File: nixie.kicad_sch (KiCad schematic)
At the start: 15 parts, among them Q1 2N3906, Q2 Q_NMOS_GDS, U1 MC34063AP

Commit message: updated power
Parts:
- added J1: Barrel_Jack, symbol Connector:Barrel_Jack
- added U2: LM7805_TO220, Package_TO_SOT_THT:TO-220-3_Vertical, symbol Regulator_Linear:LM7805_TO220
- C1: value C -> 447p
- D3: value D_TVS -> 220
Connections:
- net GND: now also J1.2, U2.2 (GND)
- net Vin: now also J1.1, U2.1 (VI)
- net V_HV renamed HV
- new net 5V: U2.3 (VO)
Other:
- note added: "Power Input 12V Output 5V and 190V"
- moved on the sheet: C1, C2, C3, D1, D2, D3, L1, Q1, Q2, R1, R2, R3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

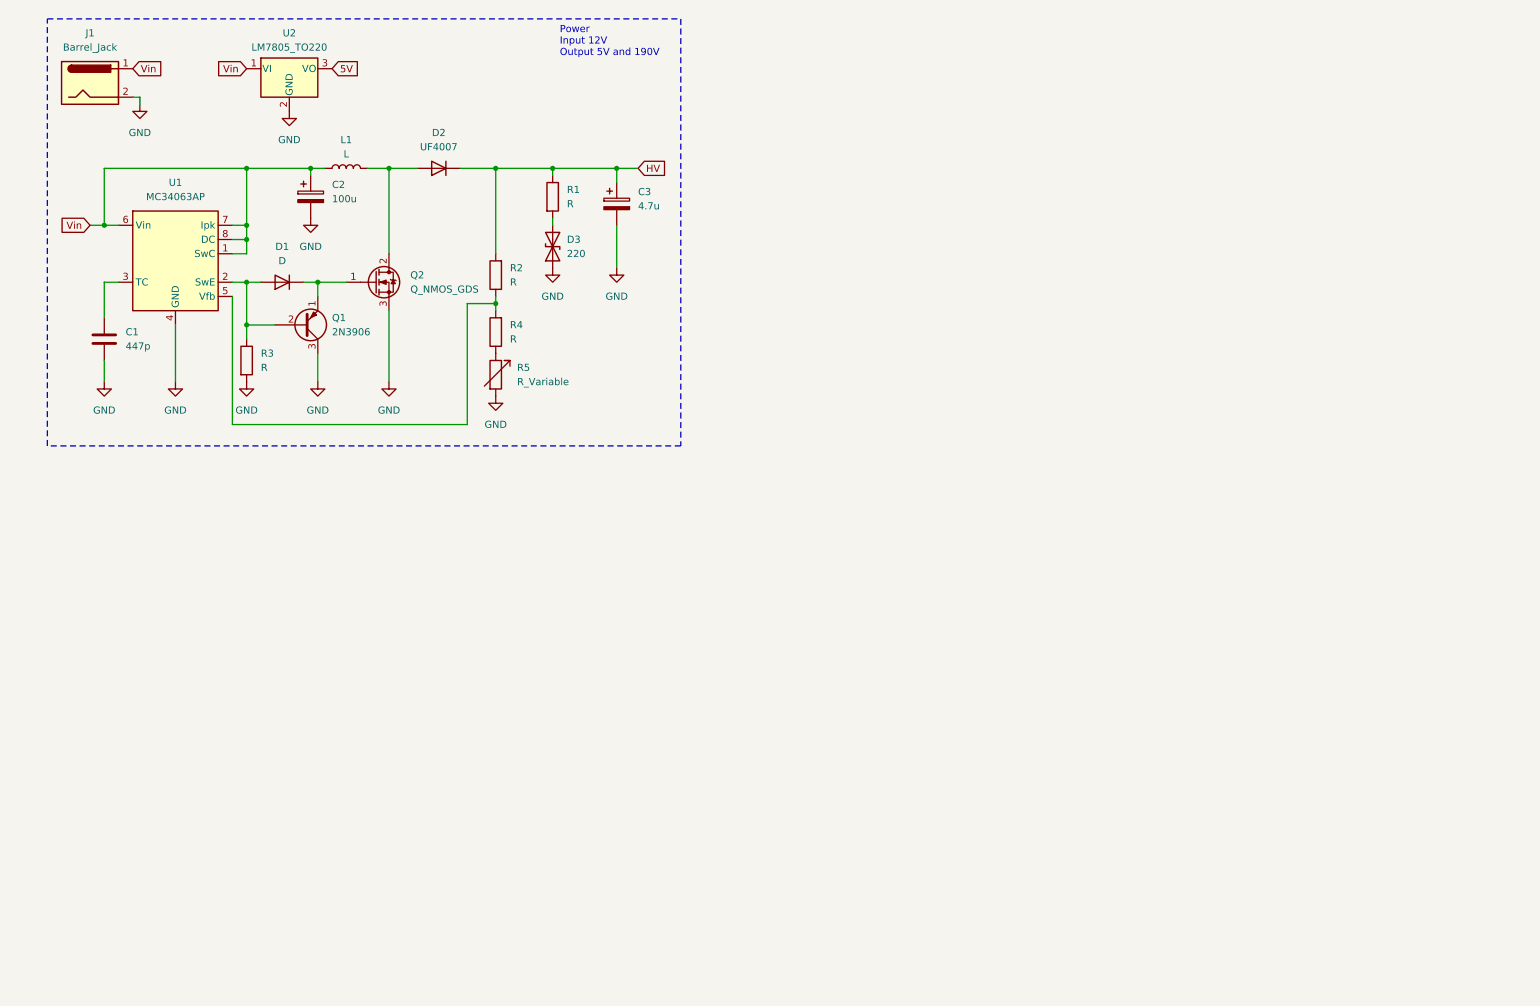
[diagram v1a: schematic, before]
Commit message: stub with nixies and drivers
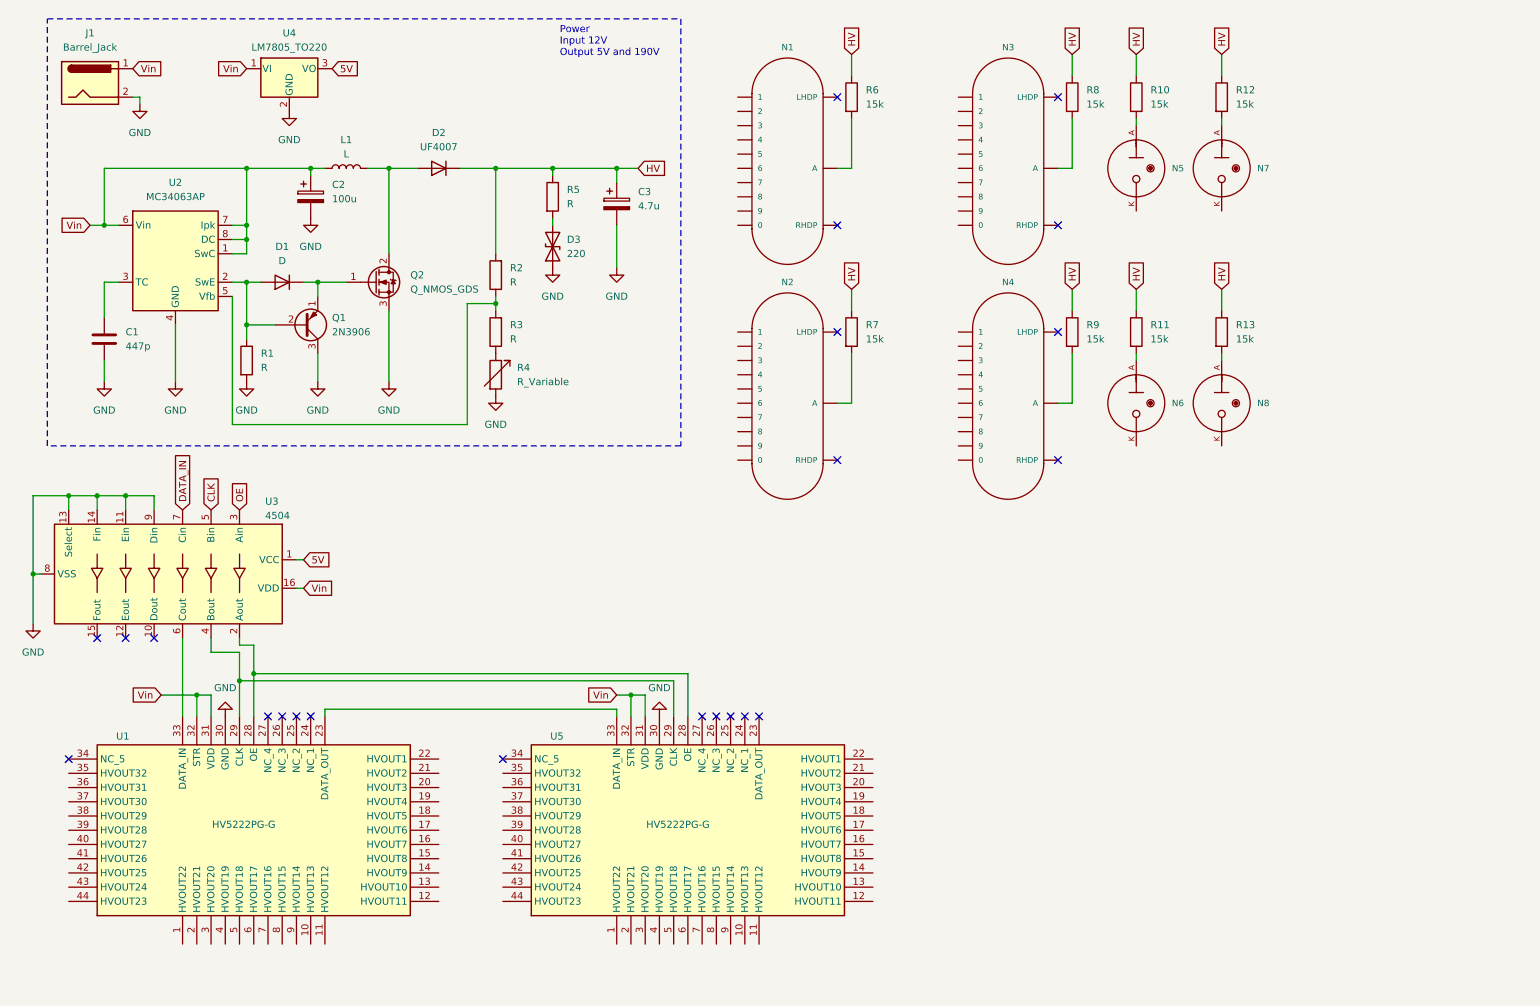
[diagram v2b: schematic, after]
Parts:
- added N1, N2, N3, N4: IN-14, nixie:nixies-us-IN-14, symbol nixie:IN-14
- added N5, N6, N7, N8: IN-3, nixie:nixies-us-IN-3, symbol nixie:IN-3
- added R10, R11, R12, R13, R6, R7, R8, R9: 15k, symbol Device:R
- added U1, U5: HV5222PG-G, Package_QFP:PQFP-44_10x10mm_P0.8mm, symbol nixie:HV5222PG-G
- added U3: 4504, Package_DIP:DIP-16_W7.62mm, symbol 4xxx:4504
- renumbered R3 to R1, R4 to R3, R5 to R4, R1 to R5, U1 to U2, U2 to U4
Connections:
- net 5V: now also U3.1 (VCC)
- net GND: now also U1.30 (GND), U3.11 (Ein), U3.13 (Select), U3.14 (Fin), U3.8 (VSS), U3.9 (Din), U5.30 (GND)
- net HV: now also R10.1, R11.1, R12.1, R13.1, R6.1, R7.1, R8.1, R9.1
- net Vin: now also U1.31 (VDD), U1.32 (STR), U3.16 (VDD), U5.31 (VDD), U5.32 (STR)
- new net: N1.A, R6.2
- new net: N7.A, R12.2
- new net: N6.A, R11.2
- new net: N2.A, R7.2
- new net: U1.23 (DATA_OUT), U5.33 (DATA_IN)
- new net: U1.28 (OE), U3.2 (Aout), U5.28 (OE)
- new net: U1.29 (CLK), U3.4 (Bout), U5.29 (CLK)
- new net: U1.33 (DATA_IN), U3.6 (Cout)
- new net: N3.A, R8.2
- new net: N8.A, R13.2
- new net: N5.A, R10.2
- new net: N4.A, R9.2
- new net CLK: U3.5 (Bin)
- new net DATA_IN: U3.7 (Cin)
- new net OE: U3.3 (Ain)
- no-connect marks 0 -> 22

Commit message: connected nixie tubes, drivers, and level shifting
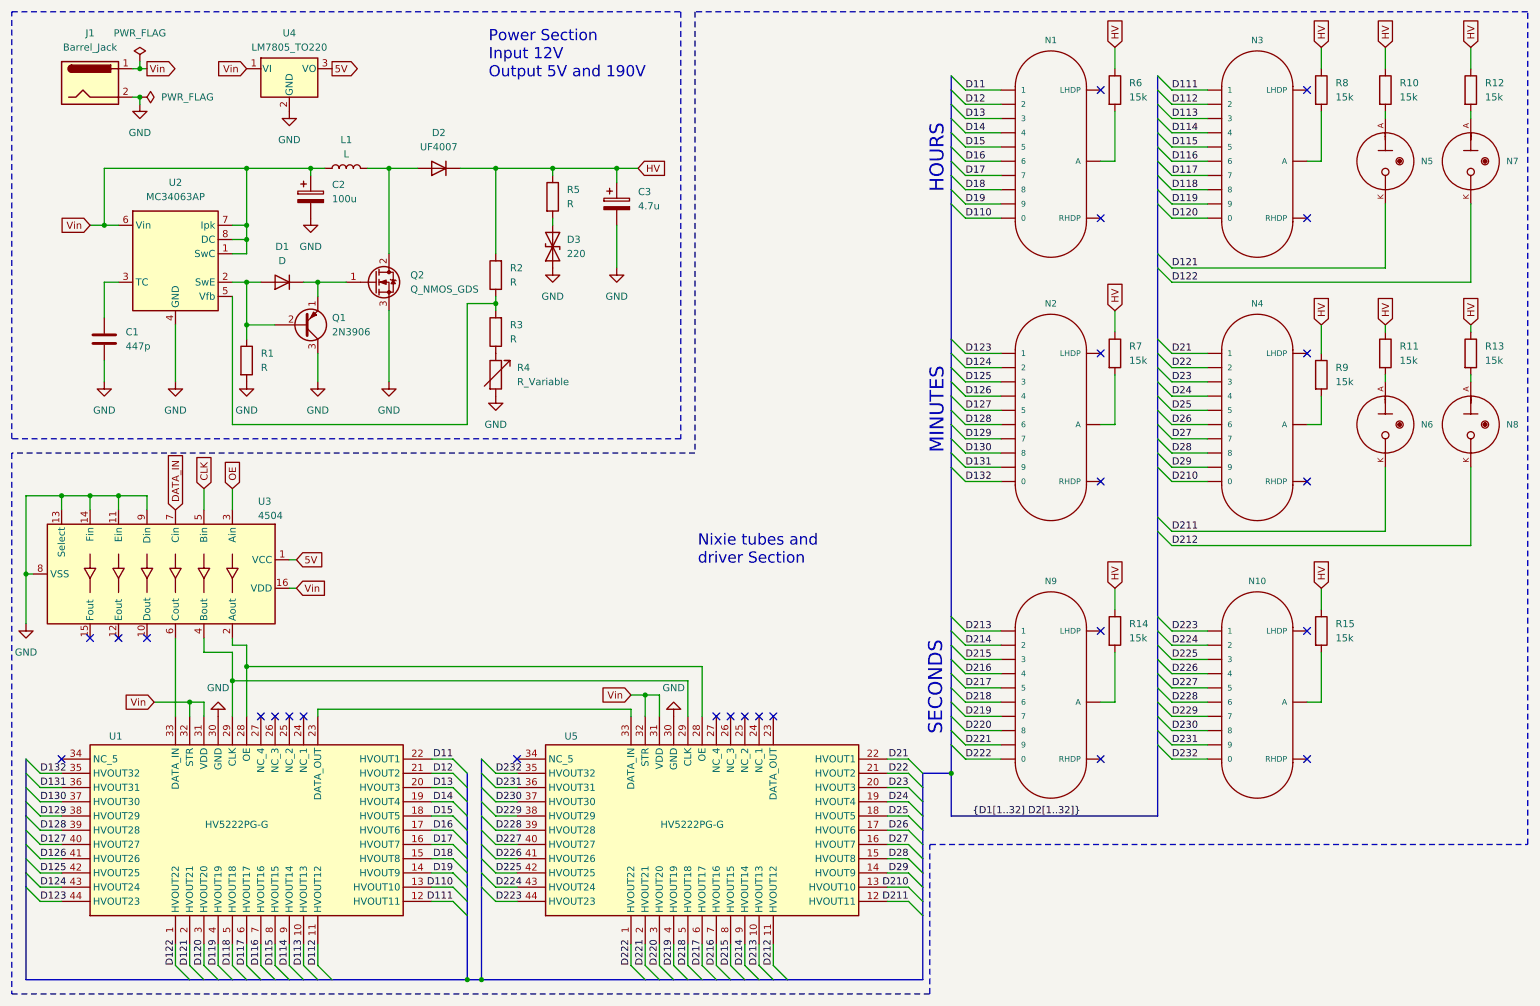
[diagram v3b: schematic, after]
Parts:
- added N10, N9: IN-14, nixie:nixies-us-IN-14, symbol nixie:IN-14
- added R14, R15: 15k, symbol Device:R
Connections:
- net HV: now also R14.1, R15.1
- net D110: now reaches N1.0
- net D110: now also U1.13 (HVOUT10)
- net D11: now reaches N1.1
- net D11: now also U1.22 (HVOUT1)
- net D12: now reaches N1.2
- net D12: now also U1.21 (HVOUT2)
- net D13: now reaches N1.3
- net D13: now also U1.20 (HVOUT3)
- net D14: now reaches N1.4
- net D14: now also U1.19 (HVOUT4)
- net D15: now reaches N1.5
- net D15: now also U1.18 (HVOUT5)
- net D16: now reaches N1.6
- net D16: now also U1.17 (HVOUT6)
- net D17: now reaches N1.7
- net D17: now also U1.16 (HVOUT7)
- net D18: now reaches N1.8
- net D18: now also U1.15 (HVOUT8)
- net D19: now reaches N1.9
- net D19: now also U1.14 (HVOUT9)
- net D211: now reaches N6.K
- net D211: now also U5.12 (HVOUT11)
- net D132: now reaches N2.0
- net D132: now also U1.35 (HVOUT32)
- net D123: now reaches N2.1
- net D123: now also U1.44 (HVOUT23)
- net D124: now reaches N2.2
- net D124: now also U1.43 (HVOUT24)
- net D125: now reaches N2.3
- net D125: now also U1.42 (HVOUT25)
- net D126: now reaches N2.4
- net D126: now also U1.41 (HVOUT26)
- net D127: now reaches N2.5
- net D127: now also U1.40 (HVOUT27)
- net D128: now reaches N2.6
- net D128: now also U1.39 (HVOUT28)
- net D129: now reaches N2.7
- net D129: now also U1.38 (HVOUT29)
- net D130: now reaches N2.8
- net D130: now also U1.37 (HVOUT30)
- net D131: now reaches N2.9
- net D131: now also U1.36 (HVOUT31)
- net D122: now reaches U1.1 (HVOUT22)
- net D122: now also N7.K
- net D113: now reaches U1.10 (HVOUT13)
- net D113: now also N3.3
- net D112: now reaches U1.11 (HVOUT12)
- net D112: now also N3.2
- net D111: now reaches U1.12 (HVOUT11)
- net D111: now also N3.1
- net D121: now reaches U1.2 (HVOUT21)
- net D121: now also N5.K
- net D120: now reaches U1.3 (HVOUT20)
- net D120: now also N3.0
- net D119: now reaches U1.4 (HVOUT19)
- net D119: now also N3.9
- net D118: now reaches U1.5 (HVOUT18)
- net D118: now also N3.8
- net D117: now reaches U1.6 (HVOUT17)
- net D117: now also N3.7
- net D116: now reaches U1.7 (HVOUT16)
- net D116: now also N3.6
- net D115: now reaches U1.8 (HVOUT15)
- net D115: now also N3.5
- net D114: now reaches U1.9 (HVOUT14)
- net D114: now also N3.4
- net D212: now reaches N8.K
- net D212: now also U5.11 (HVOUT12)
- net D210: now reaches N4.0
- net D210: now also U5.13 (HVOUT10)
- net D21: now reaches N4.1
- net D21: now also U5.22 (HVOUT1)
- net D22: now reaches N4.2
- net D22: now also U5.21 (HVOUT2)
- net D23: now reaches N4.3
- net D23: now also U5.20 (HVOUT3)
- net D24: now reaches N4.4
- net D24: now also U5.19 (HVOUT4)
- net D25: now reaches N4.5
- net D25: now also U5.18 (HVOUT5)
- net D26: now reaches N4.6
- net D26: now also U5.17 (HVOUT6)
- net D27: now reaches N4.7
- net D27: now also U5.16 (HVOUT7)
- net D28: now reaches N4.8
- net D28: now also U5.15 (HVOUT8)
- net D29: now reaches N4.9
- net D29: now also U5.14 (HVOUT9)
- net D222: now reaches U5.1 (HVOUT22)
- net D222: now also N9.0
- net D213: now reaches U5.10 (HVOUT13)
- net D213: now also N9.1
- net D221: now reaches U5.2 (HVOUT21)
- net D221: now also N9.9
- net D220: now reaches U5.3 (HVOUT20)
- net D220: now also N9.8
- net D232: now reaches U5.35 (HVOUT32)
- net D232: now also N10.0
- net D231: now reaches U5.36 (HVOUT31)
- net D231: now also N10.9
- net D230: now reaches U5.37 (HVOUT30)
- net D230: now also N10.8
- net D229: now reaches U5.38 (HVOUT29)
- net D229: now also N10.7
- net D228: now reaches U5.39 (HVOUT28)
- net D228: now also N10.6
- net D219: now reaches U5.4 (HVOUT19)
- net D219: now also N9.7
- net D227: now reaches U5.40 (HVOUT27)
- net D227: now also N10.5
- net D226: now reaches U5.41 (HVOUT26)
- net D226: now also N10.4
- net D225: now reaches U5.42 (HVOUT25)
- net D225: now also N10.3
- net D224: now reaches U5.43 (HVOUT24)
- net D224: now also N10.2
- net D223: now reaches U5.44 (HVOUT23)
- net D223: now also N10.1
- net D218: now reaches U5.5 (HVOUT18)
- net D218: now also N9.6
- net D217: now reaches U5.6 (HVOUT17)
- net D217: now also N9.5
- net D216: now reaches U5.7 (HVOUT16)
- net D216: now also N9.4
- net D215: now reaches U5.8 (HVOUT15)
- net D215: now also N9.3
- net D214: now reaches U5.9 (HVOUT14)
- net D214: now also N9.2
- new net: N10.A, R15.2
- new net: N9.A, R14.2
- no-connect marks 22 -> 26
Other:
- note added: "HOURS"
- note added: "MINUTES"
- note added: "Nixie tubes and driver Section"
- note added: "Power Section Input 12V Output 5V and 190V"
- note added: "SECONDS"
- note removed: "Power Input 12V Output 5V and 190V"
- moved on the sheet: N1, N2, N3, N4, N5, N6, N7, N8, R10, R11, R12, R13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

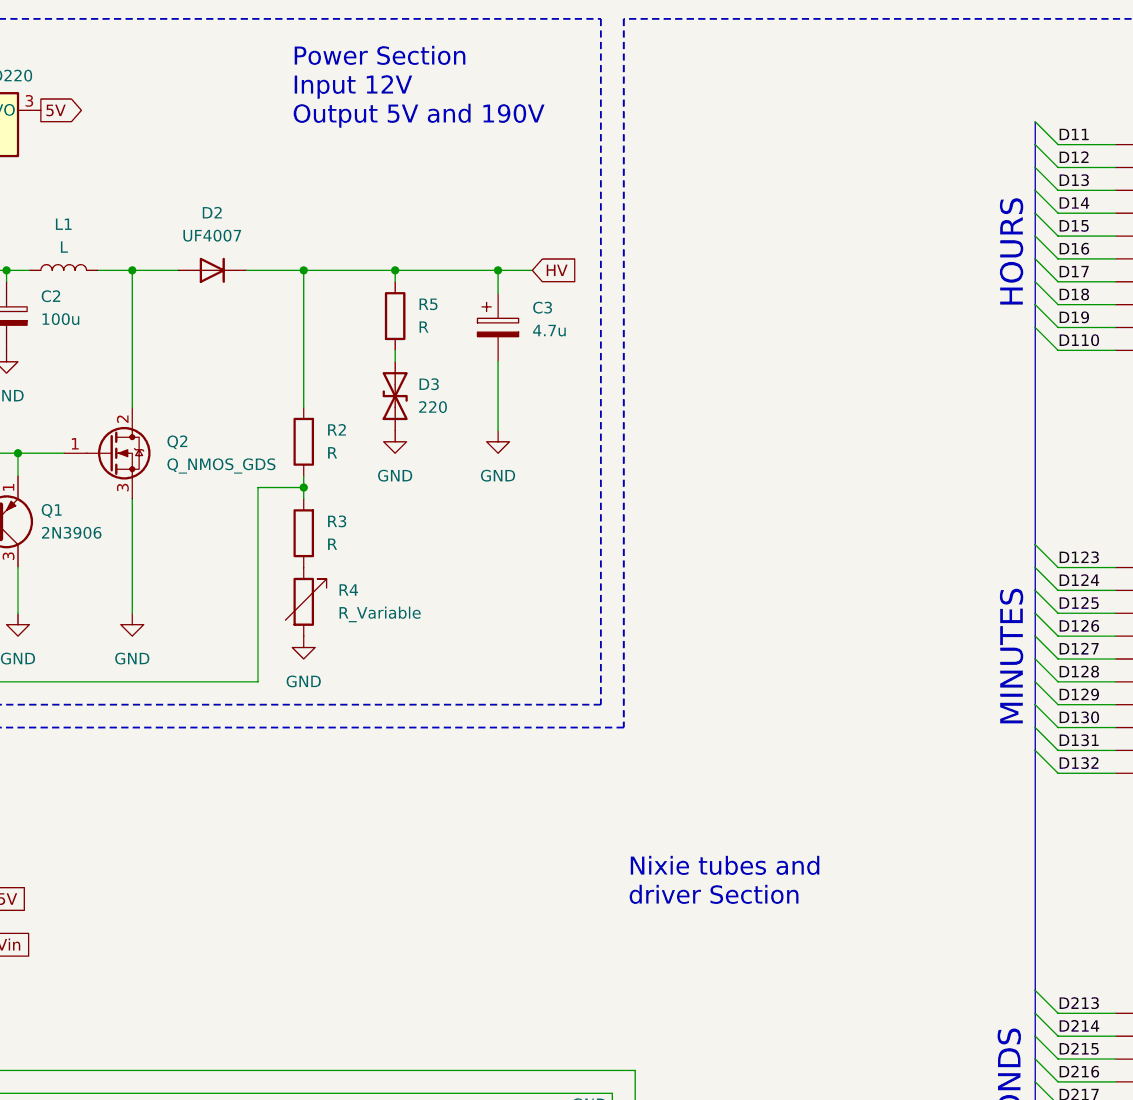
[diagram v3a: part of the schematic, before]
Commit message: added controller stub
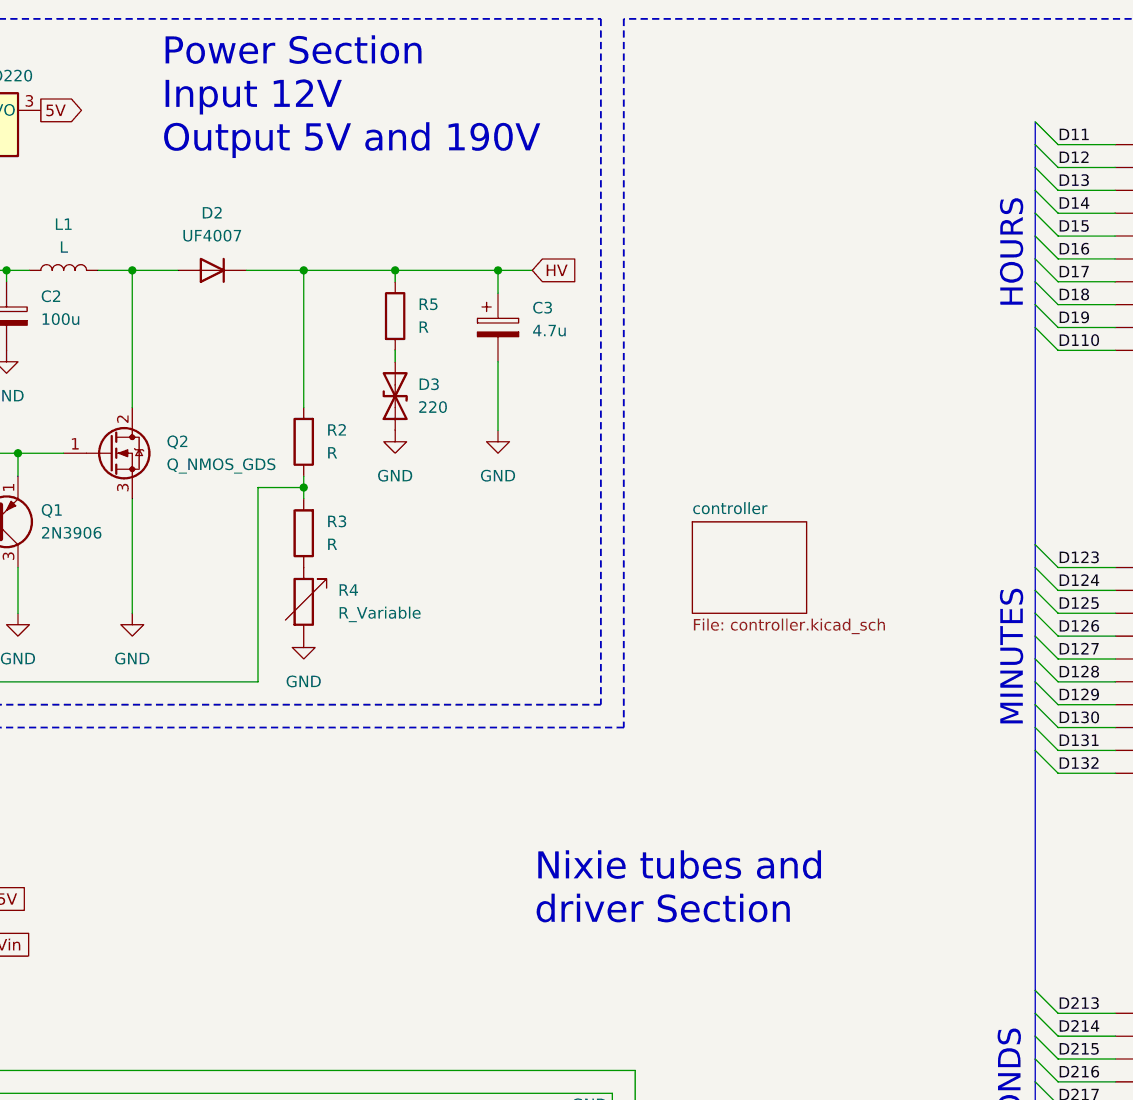
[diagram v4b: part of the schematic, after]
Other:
- added sheet controller (controller.kicad_sch)
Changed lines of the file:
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@@
 	(text "Power Section\nInput 12V\nOutput 5V and 190V"
 		(exclude_from_sim no)
-		(at 97.79 24.13 0)
+		(at 83.312 25.146 0)
 		(effects
 			(font
-				(size 2 2)
+				(size 3 3)
 			)
 			(justify left)
@@
 	(text "Nixie tubes and \ndriver Section"
 		(exclude_from_sim no)
-		(at 135.128 112.522 0)
+		(at 124.714 113.284 0)
 		(effects
 			(font
-				(size 2 2)
+				(size 3 3)
 			)
 			(justify left)
@@
 				)
 			)
+		)
+	)
+	(sheet
+		(at 142.24 72.39)
+		(size 12.7 10.16)
+		(fields_autoplaced yes)
+		(stroke
+			(width 0.1524)
+			(type solid)
+		)
+		(fill
+			(color 0 0 0 0.0000)
+		)
+		(property "Sheetname" "controller"
+			(at 142.24 71.6784 0)
+			(effects
+				(font
+					(size 1.27 1.27)
+				)
+				(justify left bottom)
+			)
+		)
+		(property "Sheetfile" "controller.kicad_sch"
+			(at 142.24 83.1346 0)
+			(effects
+				(font
+					(size 1.27 1.27)
+				)
+				(justify left top)
+			)
+		)
+		(instances
+			(project "nixie"
+				(path "/4d215aa3-d175-40c4-bbb4-87e7c6a030b1"
+					(page "2")
+				)
+			)
